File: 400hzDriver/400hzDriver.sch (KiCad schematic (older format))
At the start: 80 parts

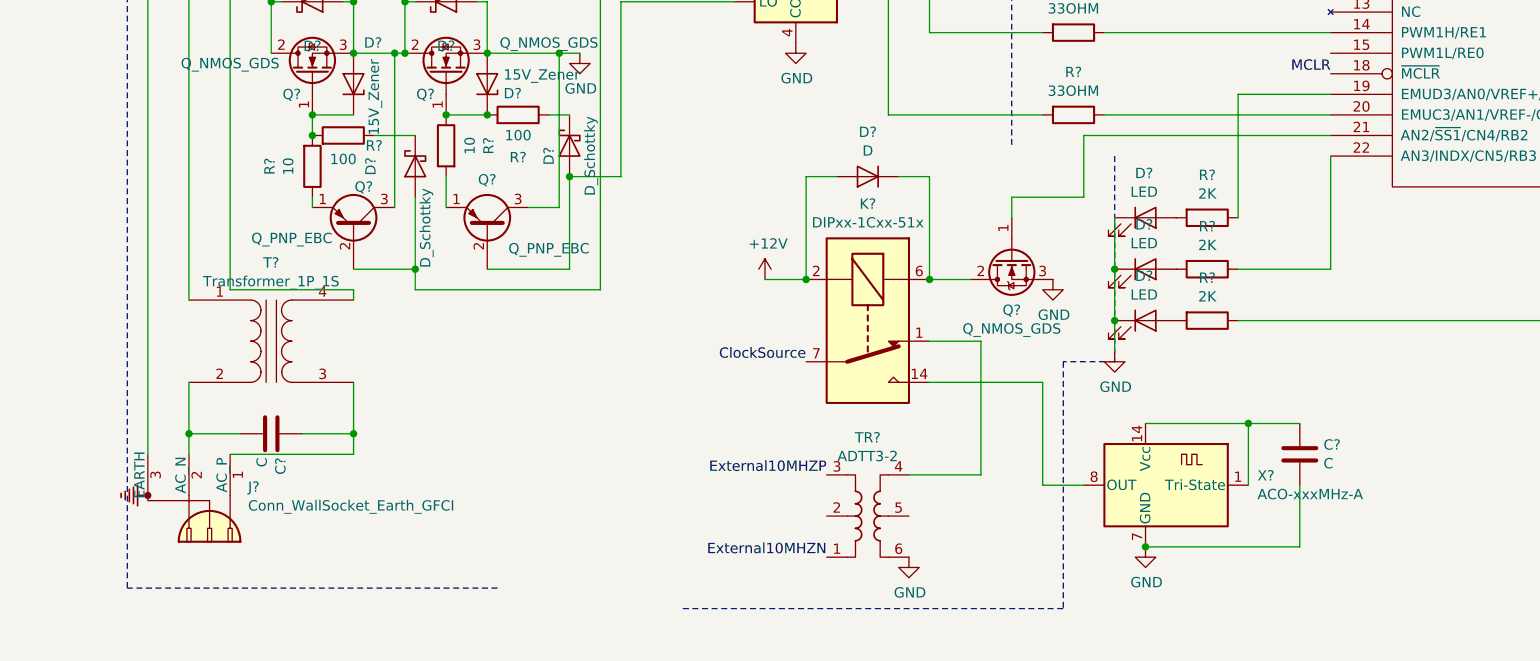
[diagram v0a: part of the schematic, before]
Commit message: Updated external 10mhz input. This has only been tested under simulation.
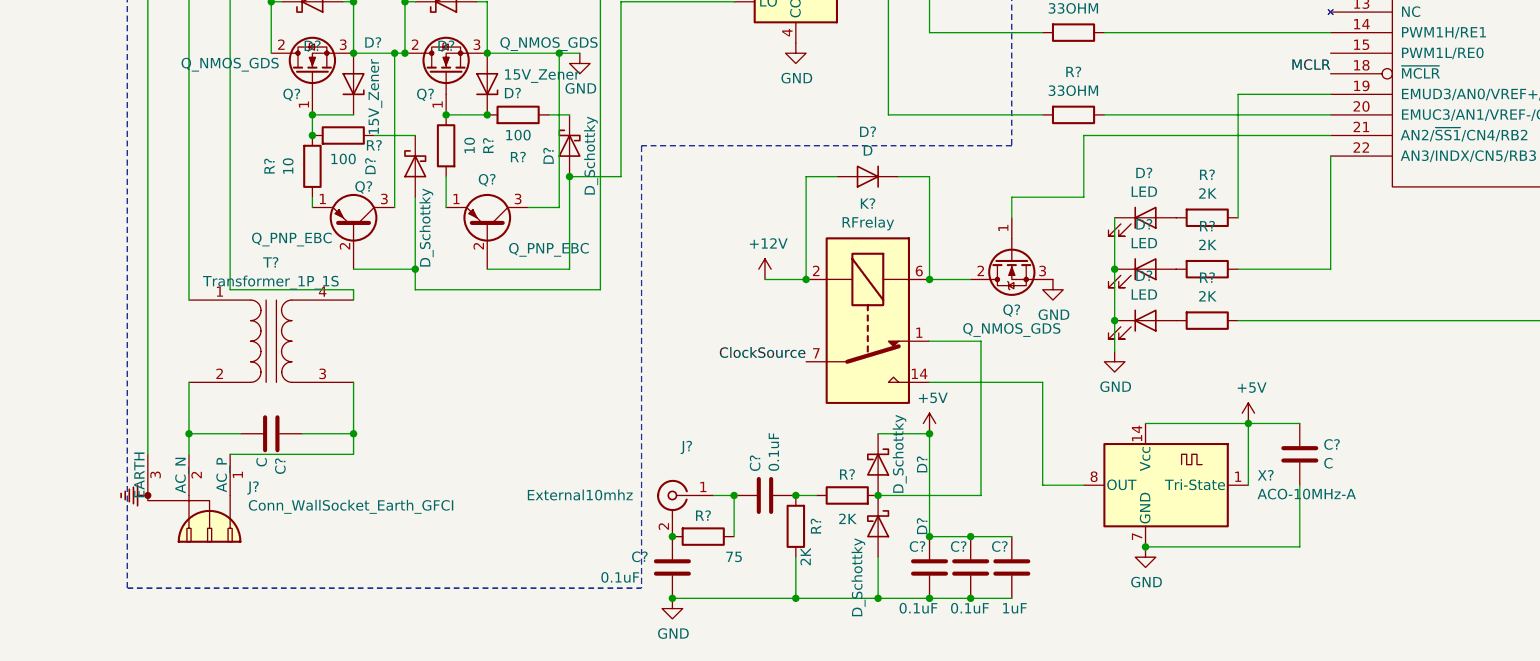
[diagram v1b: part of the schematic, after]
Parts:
- removed TR?: ADTT3-2, RF_Mini-Circuits:Mini-Circuits_CD636_H4.11mm, symbol Transformer:ADTT3-2
- added C? (x4): 0.1uF, symbol Device:C
- added C?: 1uF, symbol Device:C
- added D? (x2): D_Schottky, symbol Device:D_Schottky
- added J?: External10mhz, symbol Connector:Conn_Coaxial
- added R?: 75, symbol Device:R
- added R? (x2): 2K, symbol Device:R
- K?: value DIPxx-1Cxx-51x -> RFrelay
- X?: value ACO-xxxMHz-A -> ACO-10MHz-A
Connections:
- net +5V: now also C?.1, X?.1 (Tri-State), X?.14 (Vcc), C?.1, C?.1, C?.1, D?.1 (K)
- net GND: now also C?.2, C?.2, C?.2, C?.2, D?.2 (A), R?.1
- net at K?.1: now also D?.1 (K), D?.2 (A), R?.2
- new net: C?.1, J?.1 (In), R?.1
- new net: C?.1, J?.2 (Ext), R?.2
- new net: C?.2, R?.1, R?.2
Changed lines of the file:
@@
 P 4200 6250
 F 0 "K?" V 3633 6250 50  0000 C CNN
-F 1 "DIPxx-1Cxx-51x" V 3724 6250 50  0000 C CNN
+F 1 "RFrelay" V 3724 6250 50  0000 C CNN
 F 2 "Relay_THT:Relay_StandexMeder_DIP_LowProfile" H 4650 6200 50  0001 L CNN
 F 3 "https://standexelectronics.com/wp-content/uploads/datasheet_reed_relay_DIP.pdf" H 4200 6250 50  0001 C CNN
@@
 Text Label 10250 4950 0    50   ~ 0
 ClockSource
-$Comp
-L Transformer:ADTT3-2 TR?
-U 1 1 5FC13557
-P 4200 7200
-F 0 "TR?" H 4200 7581 50  0000 C CNN
-F 1 "ADTT3-2" H 4200 7490 50  0000 C CNN
-F 2 "RF_Mini-Circuits:Mini-Circuits_CD636_H4.11mm" H 4200 6850 50  0001 C CNN
-F 3 "https://www.minicircuits.com/pdfs/ADTT3-2+.pdf" H 4200 7200 50  0001 C CNN
-	1    4200 7200
-	1    0    0    -1
-$EndComp
-Wire Wire Line
-	4400 7000 4750 7000
-Wire Wire Line
-	4750 7000 4750 6350
 Wire Wire Line
 	4750 6350 4500 6350
-$Comp
-L power:GND #PWR?
-U 1 1 5FC17DEA
-P 4400 7400
-F 0 "#PWR?" H 4400 7150 50  0001 C CNN
-F 1 "GND" H 4405 7227 50  0000 C CNN
-F 2 "" H 4400 7400 50  0001 C CNN
-F 3 "" H 4400 7400 50  0001 C CNN
-	1    4400 7400
-	1    0    0    -1
-$EndComp
-Text Label 4000 7000 2    50   ~ 0
-External10MHZP
-Text Label 4000 7400 2    50   ~ 0
-External10MHZN
 $Comp
 L Oscillator:ACO-xxxMHz-A X?
@@
 P 5550 7050
 F 0 "X?" H 5006 7096 50  0000 R CNN
-F 1 "ACO-xxxMHz-A" H 5006 7005 50  0000 R CNN
+F 1 "ACO-10MHz-A" H 5006 7005 50  0000 R CNN
 F 2 "Oscillator:Oscillator_DIP-14" H 6000 6700 50  0001 C CNN
 F 3 "http://www.conwin.com/datasheets/cx/cx030.pdf" H 5275 7175 50  0001 C CNN
@@
 	1    0    0    -1
 $EndComp
-Wire Wire Line
-	6050 7050 6050 6750
 Wire Wire Line
 	6050 6750 5550 6750
@@
 	1700 3700 1500 3700
 Connection ~ 1500 3700
-Wire Notes Line
-	5400 5450 5400 6450
-Wire Notes Line
-	5400 6450 5150 6450
-Wire Notes Line
-	5150 6450 5150 7650
-Wire Notes Line
-	5150 7650 3300 7650
 Wire Wire Line
 	4700 4450 5050 4450
@@
 Wire Wire Line
 	5250 5350 6450 5350
-Wire Notes Line
-	2400 7550 600  7550
 Wire Notes Line
 	600  7550 600  650
@@
 	1700 4350 1700 4250
 Connection ~ 1700 4250
+$Comp
+L Connector:Conn_Coaxial J?
+U 1 1 5FC64C9C
+P 3250 7100
+F 0 "J?" H 3178 7338 50  0000 C CNN
+F 1 "External10mhz" H 3700 7100 50  0000 C CNN
+F 2 "" H 3250 7100 50  0001 C CNN
+F 3 " ~" H 3250 7100 50  0001 C CNN
+	1    3250 7100
+	-1   0    0    -1
+$EndComp
+$Comp
+L Device:C C?
+U 1 1 5FC66F0D
+P 3700 7100
+F 0 "C?" H 3815 7146 50  0000 L CNN
+F 1 "0.1uF" H 3815 7055 50  0000 L CNN
+F 2 "" H 3738 6950 50  0001 C CNN
+F 3 "~" H 3700 7100 50  0001 C CNN
+	1    3700 7100
+	0    -1   -1   0
+$EndComp
+$Comp
+L Device:C C?
+U 1 1 5FC8746F
+P 3250 7450
+F 0 "C?" H 3050 7500 50  0000 L CNN
+F 1 "0.1uF" H 2900 7400 50  0000 L CNN
+F 2 "" H 3288 7300 50  0001 C CNN
+F 3 "~" H 3250 7450 50  0001 C CNN
+	1    3250 7450
+	1    0    0    -1
+$EndComp
+$Comp
+L Device:R R?
+U 1 1 5FC87D62
+P 3400 7300
+F 0 "R?" V 3300 7300 50  0000 C CNN
+F 1 "75" V 3500 7450 50  0000 C CNN
+F 2 "" V 3330 7300 50  0001 C CNN
+F 3 "~" H 3400 7300 50  0001 C CNN
+	1    3400 7300
+	0    1    1    0
+$EndComp
+Wire Wire Line
+	3450 7100 3550 7100
+$Comp
+L power:GND #PWR?
+U 1 1 5FCBADE3
+P 3250 7600
+F 0 "#PWR?" H 3250 7350 50  0001 C CNN
+F 1 "GND" H 3255 7427 50  0000 C CNN
+F 2 "" H 3250 7600 50  0001 C CNN
+F 3 "" H 3250 7600 50  0001 C CNN
+	1    3250 7600
+	1    0    0    -1
+$EndComp
+Connection ~ 3250 7300
+Wire Wire Line
+	3550 7100 3550 7300
+Connection ~ 3550 7100
+$Comp
+L Device:R R?
+U 1 1 5FD004A9
+P 3850 7250
+F 0 "R?" V 3750 7250 50  0000 C CNN
+F 1 "2K" V 3800 7400 50  0000 C CNN
+F 2 "" V 3780 7250 50  0001 C CNN
+F 3 "~" H 3850 7250 50  0001 C CNN
+	1    3850 7250
+	-1   0    0    1
+$EndComp
+Connection ~ 3250 7600
+Wire Notes Line
+	4900 5400 3100 5400
+Wire Notes Line
+	3100 5400 3100 7550
+Wire Notes Line
+	600  7550 3100 7550
+Wire Wire Line
+	6050 7050 6050 6750
+$Comp
+L power:+5V #PWR?
+U 1 1 5FD6F14A
+P 6050 6750
+F 0 "#PWR?" H 6050 6600 50  0001 C CNN
+F 1 "+5V" H 6065 6923 50  0000 C CNN
+F 2 "" H 6050 6750 50  0001 C CNN
+F 3 "" H 6050 6750 50  0001 C CNN
+	1    6050 6750
+	1    0    0    -1
+$EndComp
+$Comp
+L power:+5V #PWR?
+U 1 1 5FD6F8F2
+P 4500 6800
+F 0 "#PWR?" H 4500 6650 50  0001 C CNN
+F 1 "+5V" H 4515 6973 50  0000 C CNN
+F 2 "" H 4500 6800 50  0001 C CNN
+F 3 "" H 4500 6800 50  0001 C CNN
+	1    4500 6800
+	1    0    0    -1
+$EndComp
+$Comp
+L Device:C C?
+U 1 1 5FD82505
+P 4500 7450
+F 0 "C?" H 4400 7550 50  0000 L CNN
+F 1 "0.1uF" H 4350 7250 50  0000 L CNN
+F 2 "" H 4538 7300 50  0001 C CNN
+F 3 "~" H 4500 7450 50  0001 C CNN
+	1    4500 7450
+	1    0    0    -1
+$EndComp
+$Comp
+L Device:C C?
+U 1 1 5FD83043
+P 4700 7450
+F 0 "C?" H 4600 7550 50  0000 L CNN
+F 1 "0.1uF" H 4600 7250 50  0000 L CNN
+F 2 "" H 4738 7300 50  0001 C CNN
+F 3 "~" H 4700 7450 50  0001 C CNN
+	1    4700 7450
+	1    0    0    -1
+$EndComp
+$Comp
+L Device:C C?
+U 1 1 5FDDC98F
+P 4900 7450
+F 0 "C?" H 4800 7550 50  0000 L CNN
+F 1 "1uF" H 4850 7250 50  0000 L CNN
+F 2 "" H 4938 7300 50  0001 C CNN
+F 3 "~" H 4900 7450 50  0001 C CNN
+	1    4900 7450
+	1    0    0    -1
+$EndComp
+Connection ~ 4700 7600
+Wire Wire Line
+	4700 7300 4900 7300
+$Comp
+L Device:R R?
+U 1 1 5FE01D58
+P 4100 7100
+F 0 "R?" V 4200 7100 50  0000 C CNN
+F 1 "2K" V 3984 7100 50  0000 C CNN
+F 2 "" V 4030 7100 50  0001 C CNN
+F 3 "~" H 4100 7100 50  0001 C CNN
+	1    4100 7100
+	0    -1   -1   0
+$EndComp
+Wire Wire Line
+	4750 7100 4750 6350
+Wire Wire Line
+	3250 7600 3850 7600
+Wire Wire Line
+	4250 6800 4500 6800
+Wire Wire Line
+	4250 7400 4250 7600
+Connection ~ 4250 7600
+Wire Wire Line
+	4250 7600 4500 7600
+Wire Wire Line
+	3950 7100 3850 7100
+Connection ~ 3850 7100
+Wire Wire Line
+	3850 7400 3850 7600
+Connection ~ 3850 7600
+Wire Wire Line
+	3850 7600 4250 7600
+Connection ~ 4500 7600
+Wire Wire Line
+	4500 7600 4700 7600
+Wire Wire Line
+	4500 7300 4500 6800
+Connection ~ 4500 6800
+Wire Wire Line
+	4750 7100 4250 7100
+Wire Wire Line
+	4700 7300 4500 7300
+Connection ~ 4700 7300
+Connection ~ 4500 7300
+Wire Wire Line
+	4900 7600 4700 7600
+$Comp
+L Device:D_Schottky D?
+U 1 1 5FEA990B
+P 4250 6950
+F 0 "D?" H 4250 7166 50  0000 C CNN
+F 1 "D_Schottky" H 4200 7050 50  0000 C CNN
+F 2 "" H 4250 6950 50  0001 C CNN
+F 3 "~" H 4250 6950 50  0001 C CNN
+	1    4250 6950
+	0    1    1    0
+$EndComp
+Connection ~ 4250 7100
+$Comp
+L Device:D_Schottky D?
+U 1 1 5FEAA3F3
+P 4250 7250
+F 0 "D?" H 4250 7466 50  0000 C CNN
+F 1 "D_Schottky" H 4500 7150 50  0000 C CNN
+F 2 "" H 4250 7250 50  0001 C CNN
+F 3 "~" H 4250 7250 50  0001 C CNN
+	1    4250 7250
+	0    1    1    0
+$EndComp
 $EndSCHEMATC

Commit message: Added resistor to make external 10mhz signal 0 point at 2.5v
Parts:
- added R?: 2K, symbol Device:R
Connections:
- net +5V: now also R?.2
- net at C?.2, R?.1, R?.2: now also R?.1
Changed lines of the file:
@@
 	0    1    1    0
 $EndComp
+$Comp
+L Device:R R?
+U 1 1 5FC57B7B
+P 3850 6950
+F 0 "R?" V 3750 7000 50  0000 C CNN
+F 1 "2K" V 3750 6850 50  0000 C CNN
+F 2 "" V 3780 6950 50  0001 C CNN
+F 3 "~" H 3850 6950 50  0001 C CNN
+	1    3850 6950
+	-1   0    0    1
+$EndComp
+Wire Wire Line
+	4250 6800 3850 6800
+Connection ~ 4250 6800
 $EndSCHEMATC

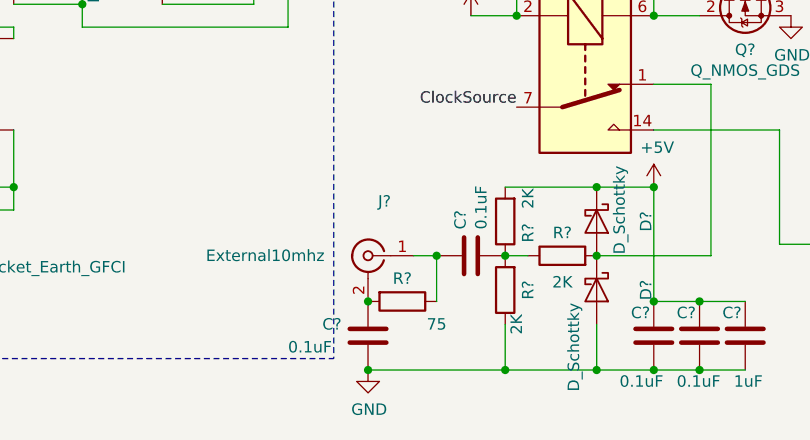
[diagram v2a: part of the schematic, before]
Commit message: Another update to external 10mhz input isolation circuit. Updated PDF schematic.
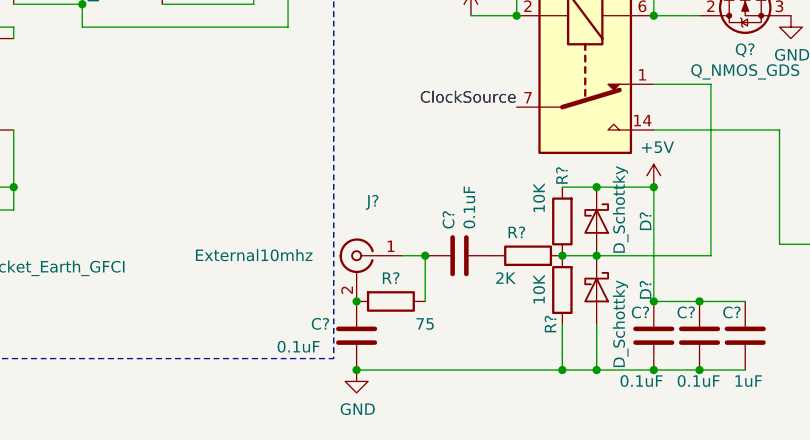
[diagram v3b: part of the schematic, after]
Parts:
- R? (x2): value 2K -> 10K
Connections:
- net at D?.1 (K), D?.2 (A), K?.1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: now also R?.1, R?.2
- net at C?.2, R?.1: no longer R?.1, R?.2
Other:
- moved on the sheet: C?, J?, R?
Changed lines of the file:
@@
 L Connector:Conn_Coaxial J?
 U 1 1 5FC64C9C
-P 3250 7100
-F 0 "J?" H 3178 7338 50  0000 C CNN
-F 1 "External10mhz" H 3700 7100 50  0000 C CNN
-F 2 "" H 3250 7100 50  0001 C CNN
-F 3 " ~" H 3250 7100 50  0001 C CNN
-	1    3250 7100
+P 3200 7100
+F 0 "J?" H 3128 7338 50  0000 C CNN
+F 1 "External10mhz" H 3650 7100 50  0000 C CNN
+F 2 "" H 3200 7100 50  0001 C CNN
+F 3 " ~" H 3200 7100 50  0001 C CNN
+	1    3200 7100
 	-1   0    0    -1
 $EndComp
@@
 L Device:C C?
 U 1 1 5FC66F0D
-P 3700 7100
-F 0 "C?" H 3815 7146 50  0000 L CNN
-F 1 "0.1uF" H 3815 7055 50  0000 L CNN
-F 2 "" H 3738 6950 50  0001 C CNN
-F 3 "~" H 3700 7100 50  0001 C CNN
-	1    3700 7100
+P 3650 7100
+F 0 "C?" H 3765 7146 50  0000 L CNN
+F 1 "0.1uF" H 3765 7055 50  0000 L CNN
+F 2 "" H 3688 6950 50  0001 C CNN
+F 3 "~" H 3650 7100 50  0001 C CNN
+	1    3650 7100
 	0    -1   -1   0
 $EndComp
@@
 L Device:C C?
 U 1 1 5FC8746F
-P 3250 7450
-F 0 "C?" H 3050 7500 50  0000 L CNN
-F 1 "0.1uF" H 2900 7400 50  0000 L CNN
-F 2 "" H 3288 7300 50  0001 C CNN
-F 3 "~" H 3250 7450 50  0001 C CNN
-	1    3250 7450
+P 3200 7450
+F 0 "C?" H 3000 7500 50  0000 L CNN
+F 1 "0.1uF" H 2850 7400 50  0000 L CNN
+F 2 "" H 3238 7300 50  0001 C CNN
+F 3 "~" H 3200 7450 50  0001 C CNN
+	1    3200 7450
 	1    0    0    -1
 $EndComp
@@
 L Device:R R?
 U 1 1 5FC87D62
-P 3400 7300
-F 0 "R?" V 3300 7300 50  0000 C CNN
-F 1 "75" V 3500 7450 50  0000 C CNN
-F 2 "" V 3330 7300 50  0001 C CNN
-F 3 "~" H 3400 7300 50  0001 C CNN
-	1    3400 7300
+P 3350 7300
+F 0 "R?" V 3250 7300 50  0000 C CNN
+F 1 "75" V 3450 7450 50  0000 C CNN
+F 2 "" V 3280 7300 50  0001 C CNN
+F 3 "~" H 3350 7300 50  0001 C CNN
+	1    3350 7300
 	0    1    1    0
 $EndComp
 Wire Wire Line
-	3450 7100 3550 7100
+	3400 7100 3500 7100
 $Comp
 L power:GND #PWR?
 U 1 1 5FCBADE3
-P 3250 7600
-F 0 "#PWR?" H 3250 7350 50  0001 C CNN
-F 1 "GND" H 3255 7427 50  0000 C CNN
-F 2 "" H 3250 7600 50  0001 C CNN
-F 3 "" H 3250 7600 50  0001 C CNN
-	1    3250 7600
-	1    0    0    -1
-$EndComp
-Connection ~ 3250 7300
-Wire Wire Line
-	3550 7100 3550 7300
-Connection ~ 3550 7100
+P 3200 7600
+F 0 "#PWR?" H 3200 7350 50  0001 C CNN
+F 1 "GND" H 3205 7427 50  0000 C CNN
+F 2 "" H 3200 7600 50  0001 C CNN
+F 3 "" H 3200 7600 50  0001 C CNN
+	1    3200 7600
+	1    0    0    -1
+$EndComp
+Connection ~ 3200 7300
+Wire Wire Line
+	3500 7100 3500 7300
+Connection ~ 3500 7100
 $Comp
 L Device:R R?
 U 1 1 5FD004A9
-P 3850 7250
-F 0 "R?" V 3750 7250 50  0000 C CNN
-F 1 "2K" V 3800 7400 50  0000 C CNN
-F 2 "" V 3780 7250 50  0001 C CNN
-F 3 "~" H 3850 7250 50  0001 C CNN
-	1    3850 7250
+P 4100 7250
+F 0 "R?" V 4150 7400 50  0000 C CNN
+F 1 "10K" V 4200 7250 50  0000 C CNN
+F 2 "" V 4030 7250 50  0001 C CNN
+F 3 "~" H 4100 7250 50  0001 C CNN
+	1    4100 7250
 	-1   0    0    1
 $EndComp
-Connection ~ 3250 7600
 Wire Notes Line
 	4900 5400 3100 5400
@@
 L Device:R R?
 U 1 1 5FE01D58
-P 4100 7100
-F 0 "R?" V 4200 7100 50  0000 C CNN
-F 1 "2K" V 3984 7100 50  0000 C CNN
-F 2 "" V 4030 7100 50  0001 C CNN
-F 3 "~" H 4100 7100 50  0001 C CNN
-	1    4100 7100
+P 3950 7100
+F 0 "R?" V 4050 7150 50  0000 C CNN
+F 1 "2K" V 3850 7200 50  0000 C CNN
+F 2 "" V 3880 7100 50  0001 C CNN
+F 3 "~" H 3950 7100 50  0001 C CNN
+	1    3950 7100
 	0    -1   -1   0
 $EndComp
 Wire Wire Line
 	4750 7100 4750 6350
-Wire Wire Line
-	3250 7600 3850 7600
 Wire Wire Line
 	4250 6800 4500 6800
@@
 Wire Wire Line
 	4250 7600 4500 7600
-Wire Wire Line
-	3950 7100 3850 7100
-Connection ~ 3850 7100
-Wire Wire Line
-	3850 7400 3850 7600
-Connection ~ 3850 7600
-Wire Wire Line
-	3850 7600 4250 7600
 Connection ~ 4500 7600
 Wire Wire Line
@@
 P 4250 7250
 F 0 "D?" H 4250 7466 50  0000 C CNN
-F 1 "D_Schottky" H 4500 7150 50  0000 C CNN
+F 1 "D_Schottky" H 4400 7350 50  0000 C CNN
 F 2 "" H 4250 7250 50  0001 C CNN
 F 3 "~" H 4250 7250 50  0001 C CNN
@@
 L Device:R R?
 U 1 1 5FC57B7B
-P 3850 6950
-F 0 "R?" V 3750 7000 50  0000 C CNN
-F 1 "2K" V 3750 6850 50  0000 C CNN
-F 2 "" V 3780 6950 50  0001 C CNN
-F 3 "~" H 3850 6950 50  0001 C CNN
-	1    3850 6950
+P 4100 6950
+F 0 "R?" V 4100 6750 50  0000 C CNN
+F 1 "10K" V 4200 6850 50  0000 C CNN
+F 2 "" V 4030 6950 50  0001 C CNN
+F 3 "~" H 4100 6950 50  0001 C CNN
+	1    4100 6950
 	-1   0    0    1
 $EndComp
 Wire Wire Line
-	4250 6800 3850 6800
+	4250 6800 4100 6800
 Connection ~ 4250 6800
+Connection ~ 4100 7100
+Wire Wire Line
+	4100 7400 4100 7600
+Connection ~ 4100 7600
+Wire Wire Line
+	4100 7600 4250 7600
+Wire Wire Line
+	4250 7100 4100 7100
+Wire Wire Line
+	3200 7600 4100 7600
+Connection ~ 3200 7600
 $EndSCHEMATC
